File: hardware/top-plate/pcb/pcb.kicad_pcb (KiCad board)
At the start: 2 copper layers, 130 x 130 mm, 81 parts, among them J1 Conn_01x02, SW1 SS-12D10L5

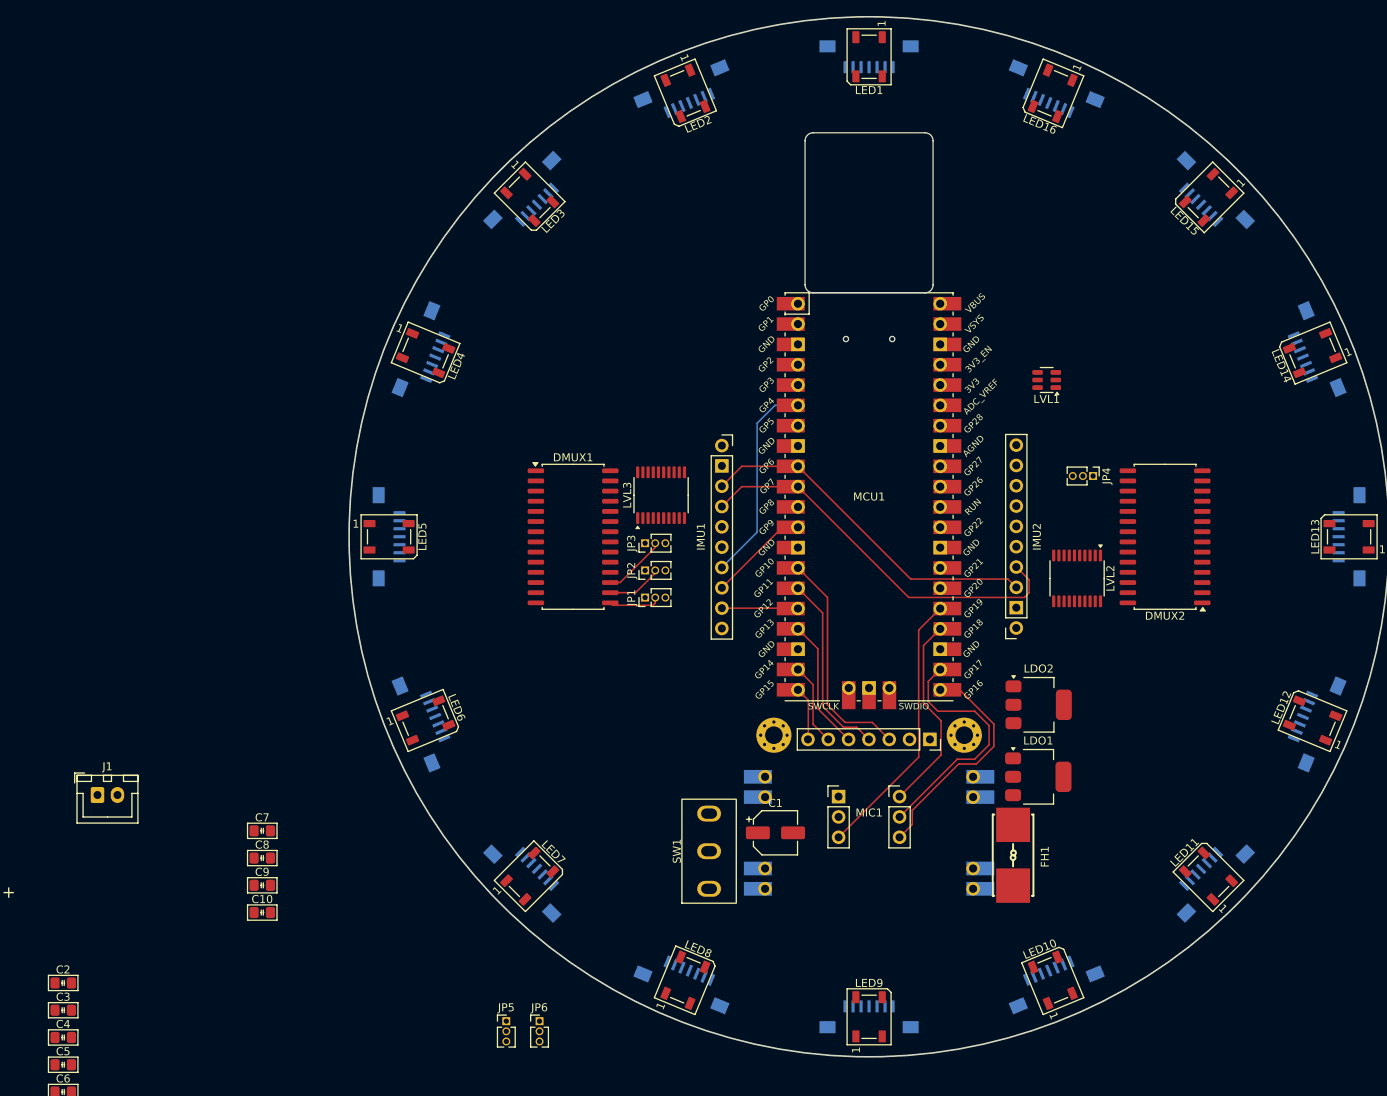
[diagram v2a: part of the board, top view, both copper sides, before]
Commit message: added fuse to bottom plate
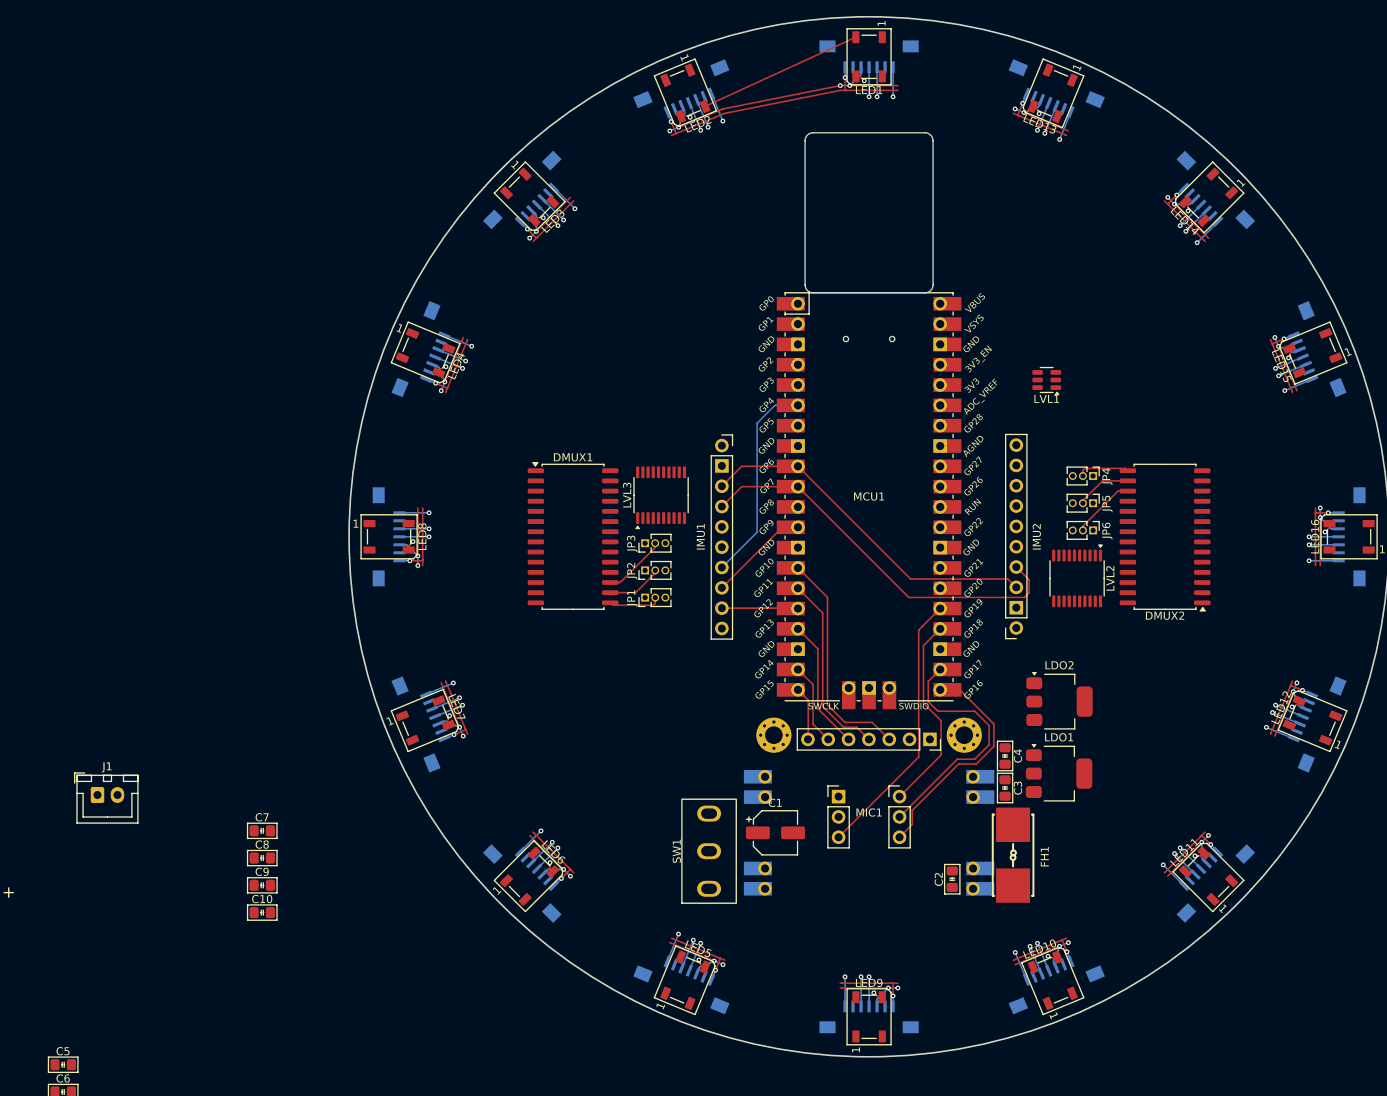
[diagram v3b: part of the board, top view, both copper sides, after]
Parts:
- moved C4 122.9 mm to (17.0, 27.4), turned to -90 degrees
- moved C3 121.0 mm to (17.0, 31.4), turned to -90 degrees
- moved C2 111.9 mm to (10.4, 42.8), turned to 90 degrees
- moved JP5 97.8 mm to (28.0, -4.20), turned to -90 degrees
- moved JP6 92.5 mm to (28.0, -0.80), turned to -90 degrees
- moved LDO1 2.63 mm to (23.8, 29.6)
- moved LDO2 2.63 mm to (23.8, 20.6)
- renumbered LED16 to LED13, LED15 to LED14, LED14 to LED15, LED13 to LED16, LED8 to LED5, LED7 to LED6, LED6 to LED7, LED5 to LED8
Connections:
- JP4 pad 1: +1V8 -> GND
- JP4 pad 3: GND -> +1V8
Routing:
- net /CH201/I2C_1V8.SCL: track 0.00 -> 179.5 mm, vias 0 -> 16
- net /CH201/I2C_1V8.SDA: track 0.00 -> 176.2 mm, vias 0 -> 32
- net +1V8: track 0.00 -> 59.2 mm, vias 0 -> 16
- net Net-(LED1-DOUT): track 0.00 -> 20.7 mm
- net GND: track 0.00 -> 20.4 mm, vias 0 -> 16
- net Net-(DMUX2-A2): track 0.00 -> 7.97 mm
- net Net-(DMUX2-A1): track 0.00 -> 6.97 mm
- net Net-(DMUX2-A0): track 0.00 -> 6.55 mm
- net /CH201/US_INT6: track 0.00 -> 3.70 mm, vias 0 -> 1
- net /CH201/US_INT2: track 0.00 -> 3.70 mm, vias 0 -> 1
- net /CH201/US_INT14: track 0.00 -> 3.70 mm, vias 0 -> 1
- net /CH201/US_INT10: track 0.00 -> 3.70 mm, vias 0 -> 1
- net /CH201/US_PROG9: track 0.00 -> 3.70 mm, vias 0 -> 1
- net /CH201/US_PROG5: track 0.00 -> 3.70 mm, vias 0 -> 1
- net /CH201/US_PROG13: track 0.00 -> 3.70 mm, vias 0 -> 1
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
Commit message: top pcb completed
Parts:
- added H10: MountingHole_Pad, MountingHole:MountingHole_2.2mm_M2_Pad_Via, F.Cu at (11.9, 59.8)
- added H11: MountingHole_Pad, MountingHole:MountingHole_2.2mm_M2_Pad_Via, F.Cu at (33.9, 50.7)
- added H12: MountingHole_Pad, MountingHole:MountingHole_2.2mm_M2_Pad_Via, F.Cu at (50.7, 33.9)
- added H13: MountingHole_Pad, MountingHole:MountingHole_2.2mm_M2_Pad_Via, F.Cu at (59.8, 11.9)
- added H14: MountingHole_Pad, MountingHole:MountingHole_2.2mm_M2_Pad_Via, F.Cu at (59.8, -11.9)
- added H15: MountingHole_Pad, MountingHole:MountingHole_2.2mm_M2_Pad_Via, F.Cu at (50.7, -33.9)
- added H16: MountingHole_Pad, MountingHole:MountingHole_2.2mm_M2_Pad_Via, F.Cu at (33.9, -50.7)
- added H17: MountingHole_Pad, MountingHole:MountingHole_2.2mm_M2_Pad_Via, F.Cu at (35.0, 16.0)
- added H18: MountingHole_Pad, MountingHole:MountingHole_2.2mm_M2_Pad_Via, F.Cu at (-32.0, 29.0)
- added H19: MountingHole_Pad, MountingHole:MountingHole_2.2mm_M2_Pad_Via, F.Cu at (-32.0, -19.0)
- added H20: MountingHole_Pad, MountingHole:MountingHole_2.2mm_M2_Pad_Via, F.Cu at (32.0, -19.0)
- added H21: MountingHole_Pad, MountingHole:MountingHole_2.2mm_M2_Pad_Via, F.Cu at (32.0, 29.0)
- added H22: MountingHole_Pad, MountingHole:MountingHole_2.2mm_M2_Pad_Via, F.Cu at (-35.0, 16.0)
- added H23: MountingHole_Pad, MountingHole:MountingHole_2.2mm_M2_Pad_Via, F.Cu at (-34.0, -27.0)
- added H24: MountingHole_Pad, MountingHole:MountingHole_2.2mm_M2_Pad_Via, F.Cu at (34.0, -27.0)
- added H9: MountingHole_Pad, MountingHole:MountingHole_2.2mm_M2_Pad_Via, F.Cu at (-11.9, 59.8)
- C1: footprint Capacitor_SMD:CP_Elec_5x5.7 -> Capacitor_SMD:CP_Elec_6.3x7.7
- MIC1: footprint INMP441:INMP441 -> INMP441:INMP441_SMD
- PWR1: value XT30-M -> Conn_01x02; footprint Connector_AMASS:AMASS_XT30U-M_1x02_P5.0mm_Vertical -> Connector_JST:JST_XH_B2B-XH-A_1x02_P2.50mm_Vertical
- moved R4 152.7 mm to (27.6, 9.80), turned to 180 degrees
- moved R1 150.9 mm to (31.6, -8.60), turned to 180 degrees
- moved R5 146.6 mm to (22.4, 7.80)
- moved H2 144.5 mm to (-11.9, -59.8)
- moved R2 144.5 mm to (25.8, -8.60)
- moved H1 142.1 mm to (11.9, -59.8)
- moved R8 139.5 mm to (22.4, -6.00), turned to -90 degrees
- moved H3 130.5 mm to (-33.9, -50.7)
- moved C6 128.2 mm to (17.0, 18.6), turned to -90 degrees
- moved J1 125.9 mm to (19.5, -16.8), turned to 90 degrees
- moved C5 125.5 mm to (17.0, 22.6), turned to 90 degrees
- moved H4 123.6 mm to (-50.7, -33.9)
- moved C9 115.4 mm to (30.2, -2.00), turned to -90 degrees
- moved C10 115.2 mm to (30.2, 2.00), turned to -90 degrees
- moved H5 103.6 mm to (-59.8, -11.9)
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- renumbered LED16 to LED13, LED15 to LED14, LED14 to LED15, LED13 to LED16, LED8 to LED5, LED7 to LED6, LED6 to LED7, LED5 to LED8
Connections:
- C2 pad 2: Net-(BUCK1-OUT+) -> +5V
- DMUX1 pad 1: /CH201/US_INT1 -> /CH201/US_PROG5
- DMUX1 pad 11: /CH201/SPI_1V8.SCS -> /CH201/SPI_1V8_1.SCS
- DMUX1 pad 12: /CH201/SPI_1V8.SCLK -> /CH201/SPI_1V8_1.SCLK
- DMUX1 pad 13: /CH201/SPI_1V8.MOSI -> /CH201/SPI_1V8_1.MOSI
- DMUX1 pad 14: /CH201/SPI_1V8.MISO -> /CH201/SPI_1V8_1.MISO
- DMUX1 pad 19: /CH201/DMUX1_INTB_1V8 -> unconnected-(DMUX1-INTB-Pad19)
- DMUX1 pad 2: /CH201/US_PROG1 -> /CH201/US_INT5
- DMUX1 pad 21: /CH201/US_INT5 -> /CH201/US_INT1
- DMUX1 pad 22: /CH201/US_PROG5 -> /CH201/US_PROG1
- DMUX1 pad 23: /CH201/US_INT6 -> /CH201/US_INT2
- DMUX1 pad 24: /CH201/US_PROG6 -> /CH201/US_PROG2
- DMUX1 pad 25: /CH201/US_INT7 -> /CH201/US_INT3
- DMUX1 pad 26: /CH201/US_PROG7 -> /CH201/US_PROG3
- DMUX1 pad 27: /CH201/US_INT8 -> /CH201/US_INT4
- DMUX1 pad 28: /CH201/US_PROG8 -> /CH201/US_PROG4
- DMUX1 pad 3: /CH201/US_INT2 -> /CH201/US_INT6
- DMUX1 pad 4: /CH201/US_PROG2 -> /CH201/US_PROG6
- DMUX1 pad 5: /CH201/US_INT3 -> /CH201/US_INT7
- DMUX1 pad 6: /CH201/US_PROG3 -> /CH201/US_PROG7
- DMUX1 pad 7: /CH201/US_INT4 -> /CH201/US_INT8
- DMUX1 pad 8: /CH201/US_PROG4 -> /CH201/US_PROG8
- DMUX2 pad 1: /CH201/US_INT9 -> /CH201/US_PROG13
- DMUX2 pad 11: /CH201/SPI_1V8.SCS -> /CH201/SPI_1V8_2.SCS
- DMUX2 pad 12: /CH201/SPI_1V8.SCLK -> /CH201/SPI_1V8_2.SCLK
- DMUX2 pad 13: /CH201/SPI_1V8.MOSI -> /CH201/SPI_1V8_2.MOSI
- DMUX2 pad 14: /CH201/SPI_1V8.MISO -> /CH201/SPI_1V8_2.MISO
- DMUX2 pad 19: /CH201/DMUX2_INTB_1V8 -> unconnected-(DMUX2-INTB-Pad19)
- DMUX2 pad 2: /CH201/US_PROG9 -> /CH201/US_INT13
- DMUX2 pad 21: /CH201/US_INT13 -> /CH201/US_INT9
- DMUX2 pad 22: /CH201/US_PROG13 -> /CH201/US_PROG9
- DMUX2 pad 23: /CH201/US_INT14 -> /CH201/US_INT10
- DMUX2 pad 24: /CH201/US_PROG14 -> /CH201/US_PROG10
- DMUX2 pad 25: /CH201/US_INT15 -> /CH201/US_INT11
- DMUX2 pad 26: /CH201/US_PROG15 -> /CH201/US_PROG11
- DMUX2 pad 27: /CH201/US_INT16 -> /CH201/US_INT12
- DMUX2 pad 28: /CH201/US_PROG16 -> /CH201/US_PROG12
- DMUX2 pad 3: /CH201/US_INT10 -> /CH201/US_INT14
- DMUX2 pad 4: /CH201/US_PROG10 -> /CH201/US_PROG14
- DMUX2 pad 5: /CH201/US_INT11 -> /CH201/US_INT15
- DMUX2 pad 6: /CH201/US_PROG11 -> /CH201/US_PROG15
- DMUX2 pad 7: /CH201/US_INT12 -> /CH201/US_INT16
- DMUX2 pad 8: /CH201/US_PROG12 -> /CH201/US_PROG16
- J1 pad 1: /EN -> /RUN
- J1 pad 2: /RUN -> /EN
- LED13 pad 2: unconnected-(LED16-DOUT-Pad2) -> Net-(LED13-DOUT)
- LED13 pad 4: Net-(LED15-DOUT) -> Net-(LED12-DOUT)
- LED14 pad 2: Net-(LED15-DOUT) -> Net-(LED14-DOUT)
- LED14 pad 4: Net-(LED14-DOUT) -> Net-(LED13-DOUT)
- LED15 pad 2: Net-(LED14-DOUT) -> Net-(LED15-DOUT)
- LED15 pad 4: Net-(LED13-DOUT) -> Net-(LED14-DOUT)
- LED16 pad 2: Net-(LED13-DOUT) -> unconnected-(LED16-DOUT-Pad2)
- LED16 pad 4: Net-(LED12-DOUT) -> Net-(LED15-DOUT)
- LED5 pad 2: Net-(LED8-DOUT) -> Net-(LED5-DOUT)
- LED5 pad 4: Net-(LED7-DOUT) -> Net-(LED4-DOUT)
- LED6 pad 2: Net-(LED7-DOUT) -> Net-(LED6-DOUT)
- LED6 pad 4: Net-(LED6-DOUT) -> Net-(LED5-DOUT)
- LED7 pad 2: Net-(LED6-DOUT) -> Net-(LED7-DOUT)
- LED7 pad 4: Net-(LED5-DOUT) -> Net-(LED6-DOUT)
- LED8 pad 2: Net-(LED5-DOUT) -> Net-(LED8-DOUT)
- LED8 pad 4: Net-(LED4-DOUT) -> Net-(LED7-DOUT)
- LVL2 pad 1: /CH201/SPI_1V8.SCS -> /CH201/DMUX1_INTA_1V8
- LVL2 pad 12: /DMUX2_NRST -> unconnected-(LVL2-B8-Pad12)
- LVL2 pad 14: /I2C1.SCL -> /DMUX_SCS
- LVL2 pad 15: /I2C1.SDA -> /SPI0.SCLK
- LVL2 pad 16: /SPI0.MISO -> /SPI0.MOSI
- LVL2 pad 17: /SPI0.MOSI -> /SPI0.MISO
- LVL2 pad 18: /SPI0.SCLK -> /US_NRST
- LVL2 pad 20: /DMUX_SCS -> /DMUX1_INTA
- LVL2 pad 3: /CH201/SPI_1V8.SCLK -> /CH201/US_NRST_1V8
- LVL2 pad 4: /CH201/SPI_1V8.MOSI -> /CH201/SPI_1V8_1.MISO
- LVL2 pad 5: /CH201/SPI_1V8.MISO -> /CH201/SPI_1V8_1.MOSI
- LVL2 pad 6: /CH201/I2C_1V8.SDA -> /CH201/SPI_1V8_1.SCLK
- LVL2 pad 7: /CH201/I2C_1V8.SCL -> /CH201/SPI_1V8_1.SCS
- LVL2 pad 9: /CH201/DMUX2_NRST_1V8 -> unconnected-(LVL2-A8-Pad9)
- LVL3 pad 1: /CH201/DMUX1_INTA_1V8 -> /CH201/I2C_1V8.SDA
- LVL3 pad 12: unconnected-(LVL3-B8-Pad12) -> /DMUX2_NRST
- LVL3 pad 13: unconnected-(LVL3-B7-Pad13) -> /DMUX2_INTA
- LVL3 pad 14: unconnected-(LVL3-B6-Pad14) -> /DMUX_SCS
- LVL3 pad 15: /US_NRST -> /SPI0.SCLK
- LVL3 pad 16: /CH201/DMUX2_INTB -> /SPI0.MOSI
- LVL3 pad 17: /DMUX2_INTA -> /SPI0.MISO
- LVL3 pad 18: /CH201/DMUX1_INTB -> /I2C0.SCL
- LVL3 pad 20: /DMUX1_INTA -> /I2C0.SDA
- LVL3 pad 3: /CH201/DMUX1_INTB_1V8 -> /CH201/I2C_1V8.SCL
- LVL3 pad 4: /CH201/DMUX2_INTA_1V8 -> /CH201/SPI_1V8_2.MISO
- LVL3 pad 5: /CH201/DMUX2_INTB_1V8 -> /CH201/SPI_1V8_2.MOSI
- LVL3 pad 6: /CH201/US_NRST_1V8 -> /CH201/SPI_1V8_2.SCLK
- LVL3 pad 7: unconnected-(LVL3-A6-Pad7) -> /CH201/SPI_1V8_2.SCS
- LVL3 pad 8: unconnected-(LVL3-A7-Pad8) -> /CH201/DMUX2_INTA_1V8
- LVL3 pad 9: unconnected-(LVL3-A8-Pad9) -> /CH201/DMUX2_NRST_1V8
- MCU1 pad 1: /DMUX1_NRST -> /LED_SIG_DIR
- MCU1 pad 11: unconnected-(MCU1-GPIO8-Pad11) -> /DMUX1_NRST
- MCU1 pad 2: /DMUX2_NRST -> /LED_SIG_3V3
- MCU1 pad 26: unconnected-(MCU1-GPIO20-Pad26) -> /I2C0.SDA
- MCU1 pad 27: unconnected-(MCU1-GPIO21-Pad27) -> /I2C0.SCL
- MCU1 pad 29: unconnected-(MCU1-GPIO22-Pad29) -> /DMUX2_NRST
- MCU1 pad 31: unconnected-(MCU1-GPIO26_ADC0-Pad31) -> /DMUX2_INTA
- MCU1 pad 32: unconnected-(MCU1-GPIO27_ADC1-Pad32) -> /IMU2.INT
- MCU1 pad 34: /DMUX1_INTA -> /IMU2.NCS
- MCU1 pad 4: unconnected-(MCU1-GPIO2-Pad4) -> /DMUX1_INTA
- MCU1 pad 5: unconnected-(MCU1-GPIO3-Pad5) -> /US_NRST
- R4 pad 2: /I2C1.SDA -> /I2C0.SDA
- R5 pad 2: /I2C1.SCL -> /I2C0.SCL
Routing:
- net +1V8: track 59.2 -> 593.3 mm, vias 16 -> 25
- net /CH201/US_NRST_1V8: track 0.00 -> 526.2 mm, vias 0 -> 35
- net /CH201/I2C_1V8.SCL: track 179.5 -> 435.2 mm, vias 16 -> 18
- net /CH201/I2C_1V8.SDA: track 176.2 -> 430.0 mm, vias 32 -> 35
- net +5V: track 0.00 -> 132.2 mm, vias 0 -> 10
- net GND: track 20.4 -> 115.5 mm, vias 16 -> 29
- net /CH201/US_INT9: track 3.70 -> 82.5 mm
- net /CH201/US_INT1: track 3.70 -> 82.5 mm
- net /CH201/US_PROG9: track 3.70 -> 81.1 mm
- net /CH201/US_PROG1: track 3.70 -> 81.1 mm
- net /DMUX_SCS: track 0.00 -> 65.1 mm
- net /CH201/US_INT2: track 3.70 -> 61.9 mm
- net /CH201/US_INT10: track 3.70 -> 61.9 mm
- net /CH201/US_PROG2: track 3.70 -> 60.9 mm
- net /CH201/US_PROG10: track 3.70 -> 60.9 mm
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- added copper zone on F.Cu, net +3V3
- added copper zone on F.Cu, net +5V
- added copper zone on B.Cu, net GND
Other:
- outline, holes or cut-outs redrawn
- board text added: "+"
- board text added: "-"
- board text added: "A0 | A1 | A2"
- board text added: "A2 | A1 | A0"
- board text added: "Features: 16 ultrasound ring RGB LEDs 2 IMUs OLED panel Microphone And way too many breakouts boards."
- board text added: "Hall of shame: ______________"
- board text added: "Interfaced via USB!"
- board text added: "RUN|EN"
- board text added: "Team BotByWire Top PCB V0.1"

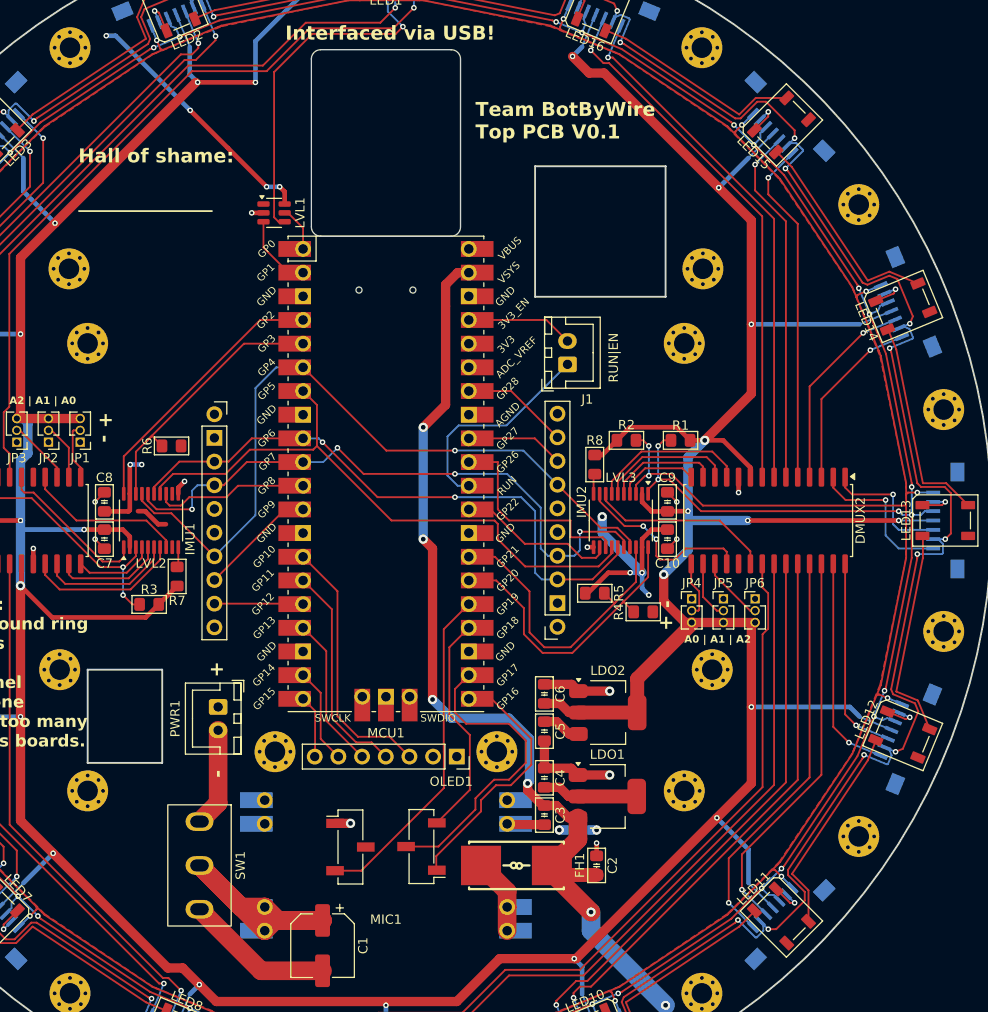
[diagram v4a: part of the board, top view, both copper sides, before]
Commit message: labelled bottom middle and top pcbs, added testpoints
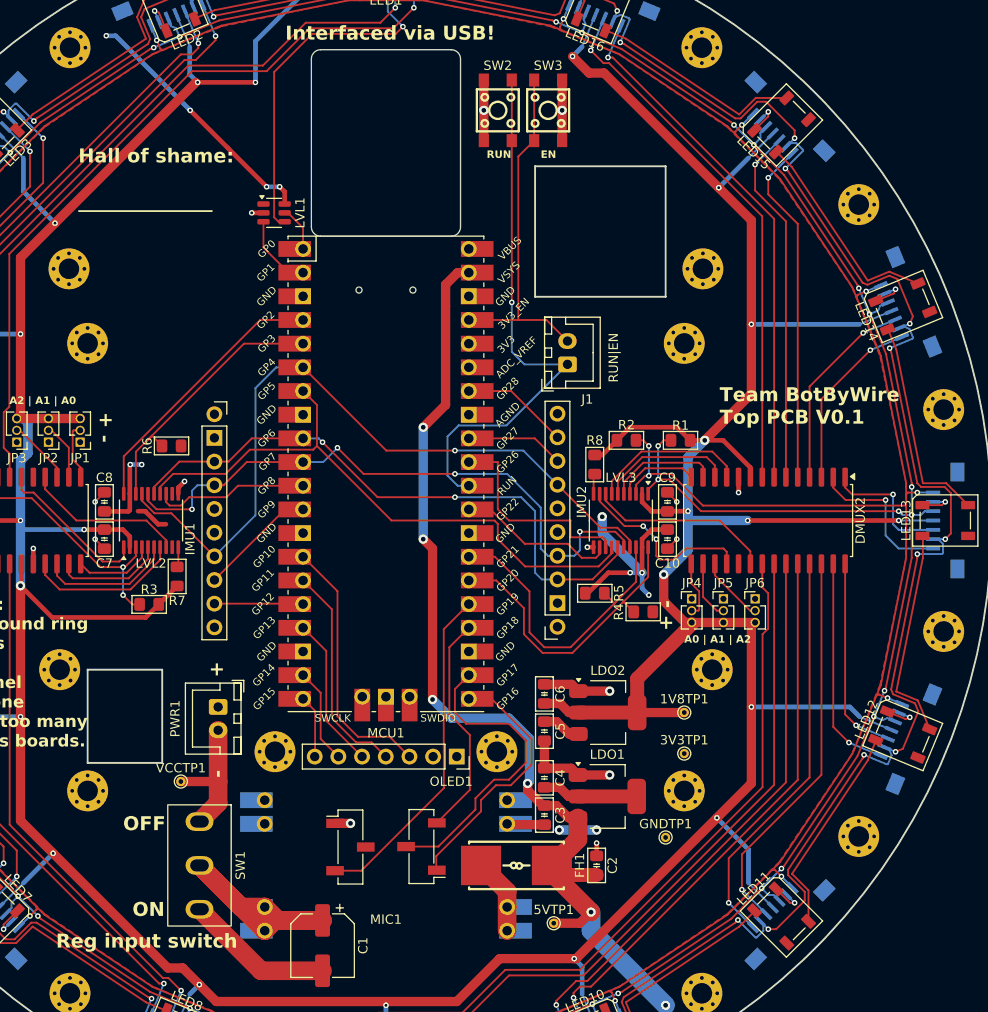
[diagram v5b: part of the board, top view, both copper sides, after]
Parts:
- added 1V8TP1: TestPoint, TestPoint:TestPoint_THTPad_D1.0mm_Drill0.5mm, F.Cu at (32.0, 20.6)
- added 3V3TP1: TestPoint, TestPoint:TestPoint_THTPad_D1.0mm_Drill0.5mm, F.Cu at (32.0, 25.0)
- added 5VTP1: TestPoint, TestPoint:TestPoint_THTPad_D1.0mm_Drill0.5mm, F.Cu at (18.0, 43.2)
- added GNDTP1: TestPoint, TestPoint:TestPoint_THTPad_D1.0mm_Drill0.5mm, F.Cu at (30.0, 34.0)
- added SW2: TS4535TP 250GF 009, EasyEDA:SW-SMD_4P-L4.5-W4.5-P3.00-LS6.8, F.Cu at (12.0, -44.0)
- added SW3: TS4535TP 250GF 009, EasyEDA:SW-SMD_4P-L4.5-W4.5-P3.00-LS6.8, F.Cu at (17.4, -44.0)
- added VCCTP1: TestPoint, TestPoint:TestPoint_THTPad_D1.0mm_Drill0.5mm, F.Cu at (-22.0, 28.0)
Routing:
- net /RUN: track 23.0 -> 58.7 mm, vias 0 -> 1
- net /EN: track 11.5 -> 38.0 mm
- net GND: track 115.5 -> 128.5 mm, vias 29 -> 31
- net +1V8: track 593.3 -> 598.4 mm
- net +5V: track 132.2 -> 136.7 mm
- net VCC: track 10.6 -> 14.6 mm
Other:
- board text added: "EN"
- board text added: "OFF"
- board text added: "ON"
- board text added: "RUN"
- board text added: "Reg input switch"

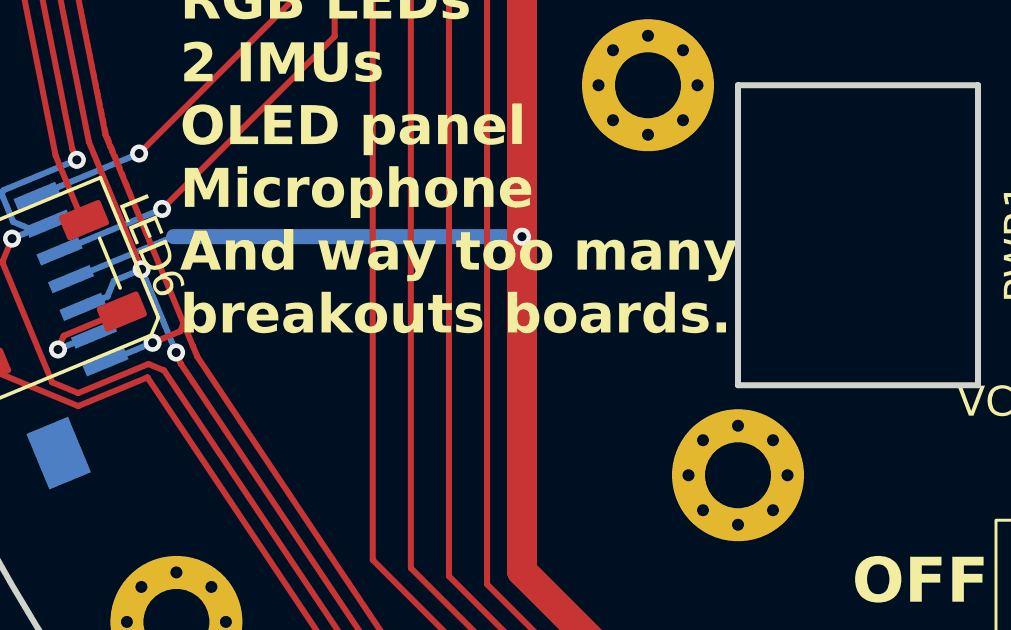
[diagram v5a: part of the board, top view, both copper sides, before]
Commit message: fixed typo in top plate
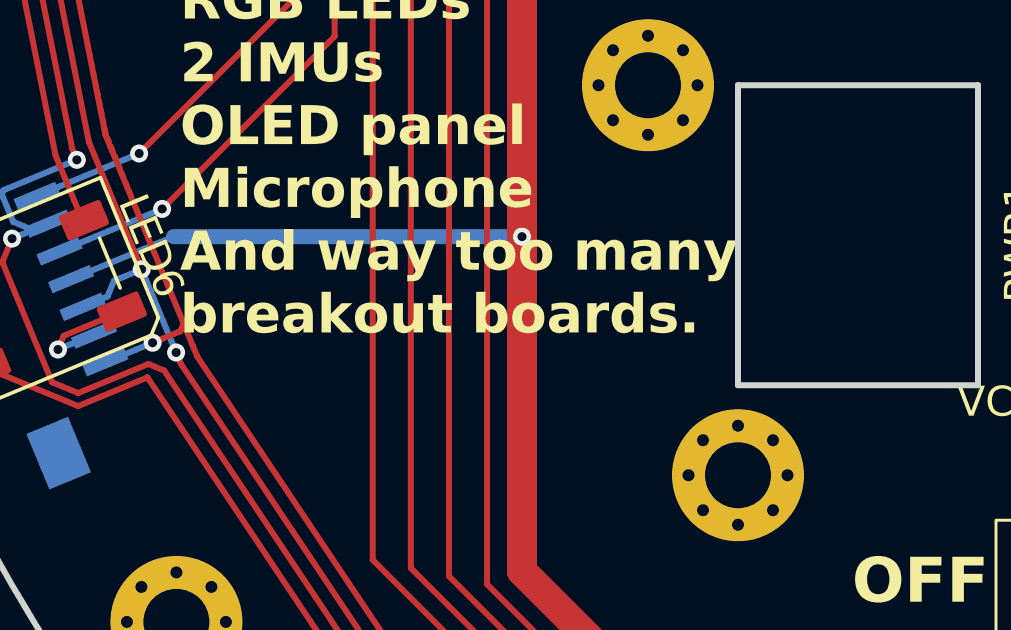
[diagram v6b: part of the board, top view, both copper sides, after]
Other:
- board text added: "Features: 16 ultrasound ring RGB LEDs 2 IMUs OLED panel Microphone And way too many breakout boards."
- board text removed: "Features: 16 ultrasound ring RGB LEDs 2 IMUs OLED panel Microphone And way too many breakouts boards."
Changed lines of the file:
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@@
 		(layer "Edge.Cuts")
 	)
-	(gr_text "Features:\n16 ultrasound ring\nRGB LEDs\n2 IMUs\nOLED panel\nMicrophone\nAnd way too many\nbreakouts boards."
+	(gr_text "Features:\n16 ultrasound ring\nRGB LEDs\n2 IMUs\nOLED panel\nMicrophone\nAnd way too many\nbreakout boards."
 		(at -50.6 24.4 0)
 		(layer "F.SilkS")
